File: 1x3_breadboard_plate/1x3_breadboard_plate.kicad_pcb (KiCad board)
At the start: 2 copper layers, 69.7 x 22 mm, 4 parts

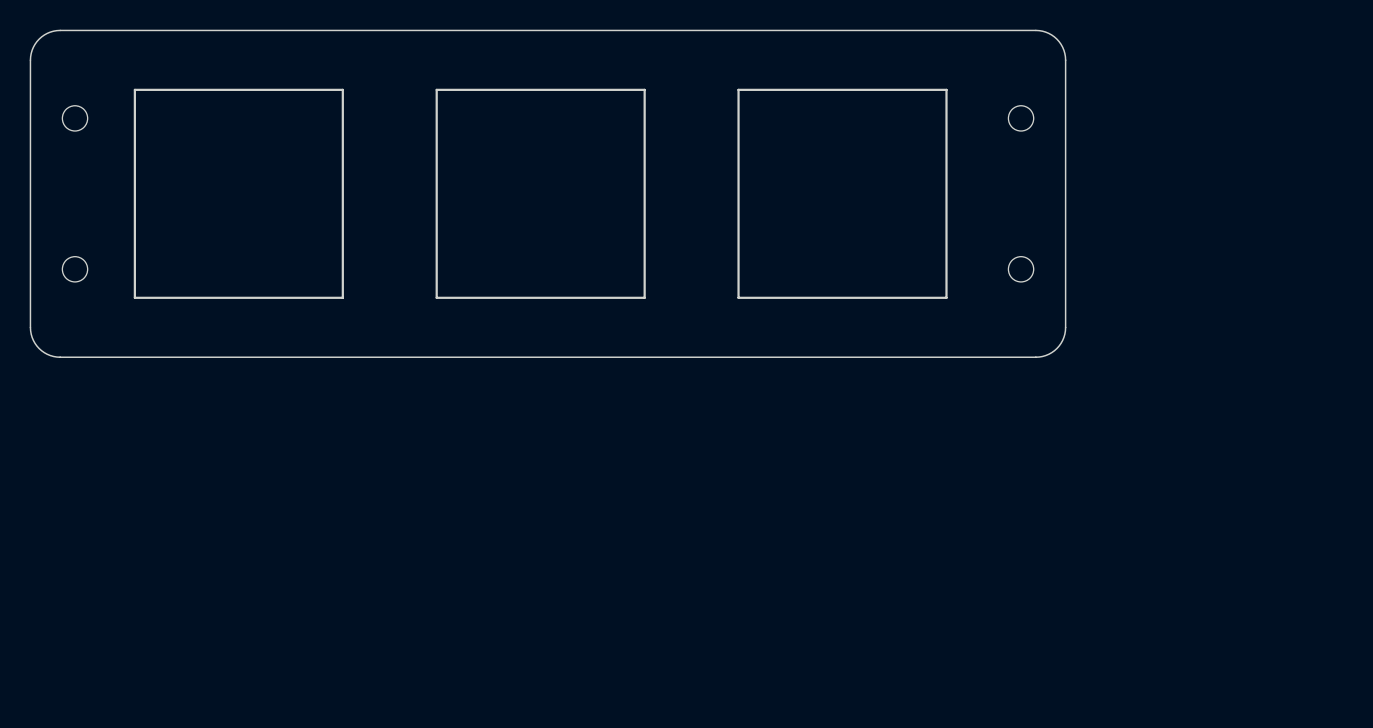
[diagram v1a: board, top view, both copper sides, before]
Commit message: fix edge cuts
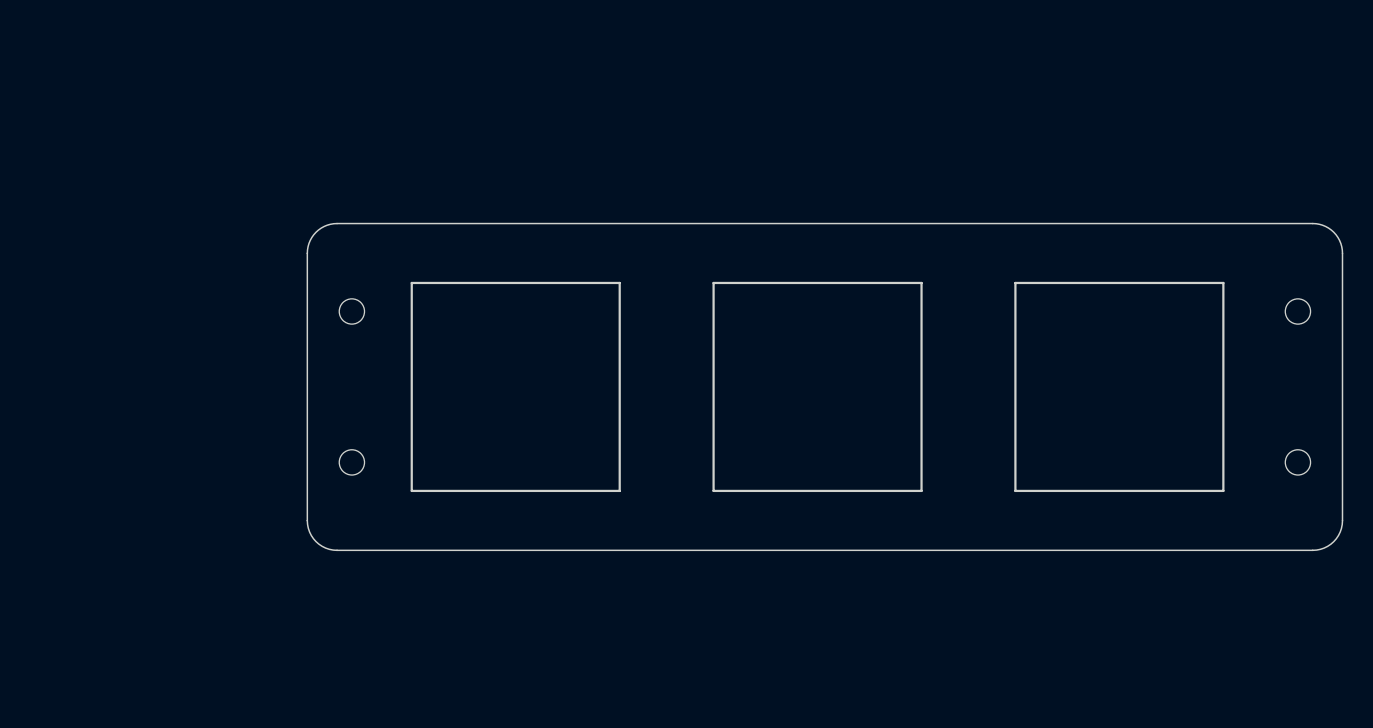
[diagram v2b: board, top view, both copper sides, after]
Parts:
- moved H1 22.7 mm to (174.7, 99.1)
- moved H2 22.7 mm to (174.7, 88.9)
- moved H1 22.7 mm to (111.0, 88.9)
- moved H2 22.7 mm to (111.0, 99.1)
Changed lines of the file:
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@@
   (net 0 "")
   (footprint "PCM_kikit:NPTH" (layer "F.Cu")
-    (at 156.019567 75.92 180)
+    (at 174.659567 88.92 180)
     (attr through_hole)
     (fp_text reference "H2" (at 0 0.5) (layer "F.SilkS") hide
@@
   )
   (footprint "PCM_kikit:NPTH" (layer "F.Cu")
-    (at 92.329567 86.08)
+    (at 110.969567 99.08)
     (attr through_hole)
     (fp_text reference "H2" (at 0 0.5) (layer "F.SilkS") hide
@@
   )
   (footprint "PCM_kikit:NPTH" (layer "F.Cu")
-    (at 92.329567 75.92)
+    (at 110.969567 88.92)
     (attr through_hole)
     (fp_text reference "H1" (at 0 0.5) (layer "F.SilkS") hide
@@
   )
   (footprint "PCM_kikit:NPTH" (layer "F.Cu")
-    (at 156.019567 86.08 180)
+    (at 174.659567 99.08 180)
     (attr through_hole)
     (fp_text reference "H1" (at 0 0.5) (layer "F.SilkS") hide
@@
     (pad "" np_thru_hole circle (at 0 0 180) (size 1.7 1.7) (drill 1.7) (layers "*.Mask"))
   )
-  (gr_arc (start 89.329567 72) (mid 89.915353 70.585786) (end 91.329567 70)
+  (gr_line (start 132.5 116.5) (end 125.5 116.5)
+    (stroke (width 0.15) (type default)) (layer "Cmts.User"))
+  (gr_arc (start 107.969567 85) (mid 108.555351 83.585775) (end 109.969567 83)
     (stroke (width 0.1) (type default)) (layer "Edge.Cuts"))
-  (gr_rect (start 137 74) (end 151 88)
+  (gr_rect (start 155.64 87) (end 169.64 101)
     (stroke (width 0.15) (type default)) (fill none) (layer "Edge.Cuts"))
-  (gr_arc (start 157.019567 70) (mid 158.433781 70.585786) (end 159.019567 72)
+  (gr_arc (start 175.659567 83) (mid 177.073802 83.585775) (end 177.659567 85)
     (stroke (width 0.1) (type default)) (layer "Edge.Cuts"))
-  (gr_arc (start 91.329567 92) (mid 89.915353 91.414214) (end 89.329567 90)
+  (gr_arc (start 109.969567 105) (mid 108.555375 104.414202) (end 107.969567 103)
     (stroke (width 0.1) (type default)) (layer "Edge.Cuts"))
-  (gr_rect (start 116.68 74) (end 130.68 88)
+  (gr_rect (start 135.32 87) (end 149.32 101)
     (stroke (width 0.15) (type default)) (fill none) (layer "Edge.Cuts"))
-  (gr_line (start 159.019567 72) (end 159.019567 90)
+  (gr_line (start 177.659567 85) (end 177.659567 103)
     (stroke (width 0.1) (type default)) (layer "Edge.Cuts"))
-  (gr_line (start 157.019567 92) (end 91.329567 92)
+  (gr_line (start 175.659567 105) (end 109.969567 105)
     (stroke (width 0.1) (type default)) (layer "Edge.Cuts"))
-  (gr_line (start 157.019567 70) (end 91.329567 70)
+  (gr_line (start 175.659567 83) (end 109.969567 83)
     (stroke (width 0.1) (type default)) (layer "Edge.Cuts"))
-  (gr_line (start 89.329567 90) (end 89.329567 72)
+  (gr_line (start 107.969567 103) (end 107.969567 85)
     (stroke (width 0.1) (type default)) (layer "Edge.Cuts"))
-  (gr_rect (start 96.36 74) (end 110.36 88)
+  (gr_rect (start 115 87) (end 129 101)
     (stroke (width 0.15) (type default)) (fill none) (layer "Edge.Cuts"))
-  (gr_arc (start 159.019567 90) (mid 158.433781 91.414214) (end 157.019567 92)
+  (gr_arc (start 177.659567 103) (mid 177.073779 104.414202) (end 175.659567 105)
     (stroke (width 0.1) (type default)) (layer "Edge.Cuts"))
-  (gr_rect (start 134.5 71.5) (end 153.5 90.5)
+  (gr_rect (start 153.14 84.5) (end 172.14 103.5)
     (stroke (width 0.15) (type default)) (fill none) (layer "Margin"))
-  (gr_rect (start 114.18 71.5) (end 133.18 90.5)
+  (gr_rect (start 132.82 84.5) (end 151.82 103.5)
     (stroke (width 0.15) (type default)) (fill none) (layer "Margin"))
-  (gr_rect (start 93.86 71.5) (end 112.86 90.5)
+  (gr_rect (start 112.5 84.5) (end 131.5 103.5)
     (stroke (width 0.15) (type default)) (fill none) (layer "Margin"))
   (zone (net 0) (net_name "") (layers "*.Mask") (hatch edge 0.5)
@@
     (polygon
       (pts
-        (xy 88 69)
-        (xy 160 69)
-        (xy 160 93)
-        (xy 88 93)
+        (xy 106.64 82)
+        (xy 178.64 82)
+        (xy 178.64 106)
+        (xy 106.64 106)
       )
     )
   )
+  (group "" (id 43b9f617-f1b2-4520-bd50-91c62da49f0e)
+    (members
+      08055c05-5de9-4a9a-a119-e19922f812c5
+      0c5f41b3-e783-4dd7-939f-8dc3d2f3ff16
+      0cdfaec3-df83-4063-ae9b-9c17142b638e
+      1a4d4f11-aa7d-4fc0-be73-470c515281a9
+      1d7a2f89-f8f4-42df-abcb-455d9649701f
+      1e90237b-85d3-4db1-a25b-07ff1cf9bf3d
+      20f8baa1-8277-4e1f-a2aa-e9319386b823
+      464e8390-9fa7-403f-ba47-4df8c322ba8b
+      5beeab23-33cb-489e-b2ee-b214e10dc540
+      71177536-c8da-41c0-92df-2cd679bc19a1
+      7d587eb0-fa47-4276-a1d8-4a22aa9f8cda
+      95e1f511-9467-4336-b604-bae186bff3ac
+      bbf3ed6e-a8e5-489c-b028-359fa569b26d
+      c9f48060-15a8-468f-8f92-c5c4dbfee1d4
+      d51c04ed-ed02-432d-bfae-dc32dd3a883f
+      da861a6b-2ef2-49cd-9050-5daf707b11a6
+      e77cc2ee-4b33-4c7b-acb0-b8ec7a6cb619
+      fd62dd3c-2c75-42d3-b98c-8bed5c4f85e8
+      fef4e613-db41-47a0-8e3a-a29de8d9e7df
+    )
+  )

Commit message: updates 1x3 breadboard plate for new dimensions
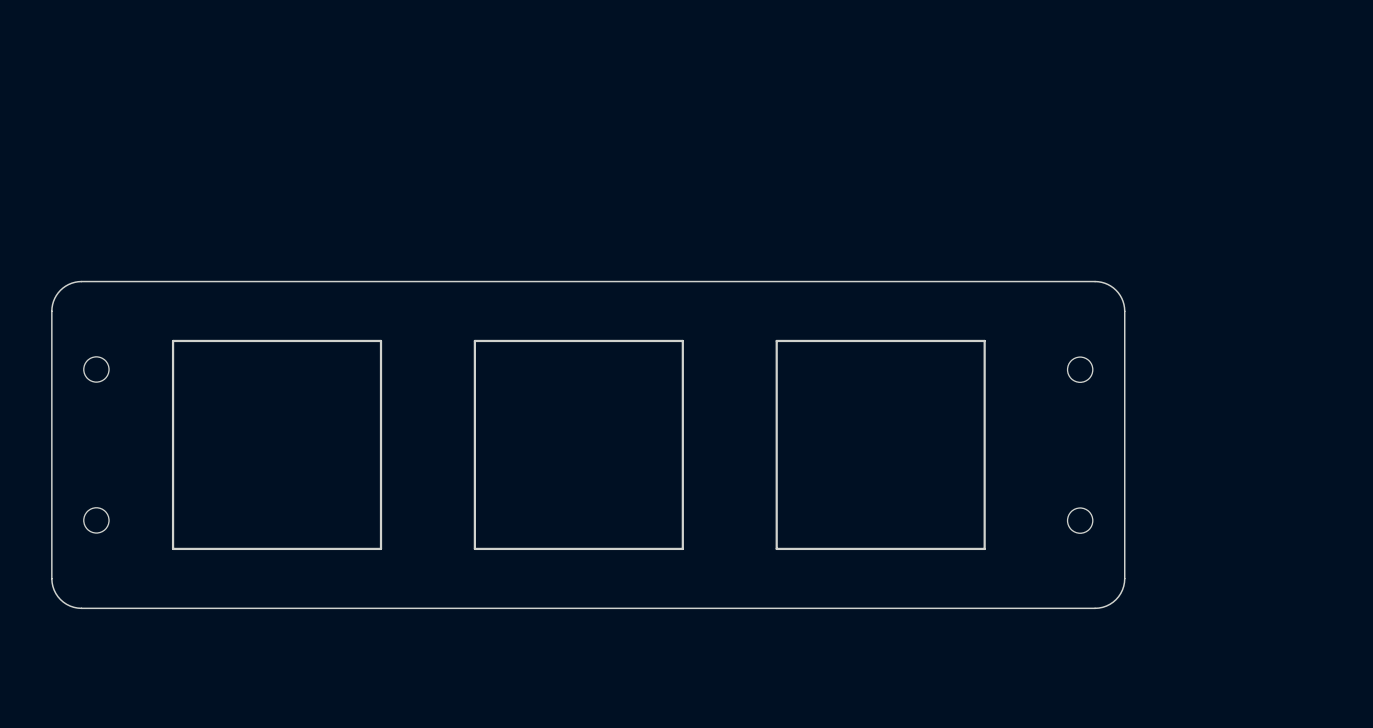
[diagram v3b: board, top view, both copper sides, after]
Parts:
- removed the H1 at (111.0, 88.9)
- removed the H1 at (174.7, 99.1)
- removed the H2 at (174.7, 88.9)
- removed the H2 at (111.0, 99.1)
- added H1: NPTH, PCM_kikit:NPTH, F.Cu at (93.8, 92.8)
- added H2: NPTH, PCM_kikit:NPTH, F.Cu at (93.8, 103.0)
- added H3: NPTH, PCM_kikit:NPTH, F.Cu at (160.0, 92.8)
- added H4: NPTH, PCM_kikit:NPTH, F.Cu at (160.0, 103.0)
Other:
- board size 69.7 x 22 mm -> 72.2 x 22 mm
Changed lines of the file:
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@@
   (net 0 "")
   (footprint "PCM_kikit:NPTH" (layer "F.Cu")
-    (at 174.659567 88.92 180)
+    (at 160 103)
     (attr through_hole)
-    (fp_text reference "H2" (at 0 0.5) (layer "F.SilkS") hide
+    (fp_text reference "H4" (at 0 0.5) (layer "F.SilkS") hide
         (effects (font (size 1 1) (thickness 0.15)))
     )
@@
         (effects (font (size 1 1) (thickness 0.15)))
     )
-    (pad "" np_thru_hole circle (at 0 0 180) (size 1.7 1.7) (drill 1.7) (layers "*.Mask"))
+    (pad "" np_thru_hole circle (at 0 0) (size 1.7 1.7) (drill 1.7) (layers "*.Mask"))
   )
   (footprint "PCM_kikit:NPTH" (layer "F.Cu")
-    (at 110.969567 99.08)
+    (at 93.77 92.825)
+    (attr through_hole)
+    (fp_text reference "H1" (at 0 0.5) (layer "F.SilkS") hide
+        (effects (font (size 1 1) (thickness 0.15)))
+    )
+    (fp_text value "NPTH" (at 0 -0.5) (layer "F.Fab") hide
+        (effects (font (size 1 1) (thickness 0.15)))
+    )
+    (pad "" np_thru_hole circle (at 0 0) (size 1.7 1.7) (drill 1.7) (layers "*.Mask"))
+  )
+  (footprint "PCM_kikit:NPTH" (layer "F.Cu")
+    (at 93.77 102.985)
     (attr through_hole)
     (fp_text reference "H2" (at 0 0.5) (layer "F.SilkS") hide
@@
   )
   (footprint "PCM_kikit:NPTH" (layer "F.Cu")
-    (at 110.969567 88.92)
+    (at 160 92.84)
     (attr through_hole)
-    (fp_text reference "H1" (at 0 0.5) (layer "F.SilkS") hide
+    (fp_text reference "H3" (at 0 0.5) (layer "F.SilkS") hide
         (effects (font (size 1 1) (thickness 0.15)))
     )
@@
     (pad "" np_thru_hole circle (at 0 0) (size 1.7 1.7) (drill 1.7) (layers "*.Mask"))
   )
-  (footprint "PCM_kikit:NPTH" (layer "F.Cu")
-    (at 174.659567 99.08 180)
-    (attr through_hole)
-    (fp_text reference "H1" (at 0 0.5) (layer "F.SilkS") hide
-        (effects (font (size 1 1) (thickness 0.15)))
-    )
-    (fp_text value "NPTH" (at 0 -0.5) (layer "F.Fab") hide
-        (effects (font (size 1 1) (thickness 0.15)))
-    )
-    (pad "" np_thru_hole circle (at 0 0 180) (size 1.7 1.7) (drill 1.7) (layers "*.Mask"))
-  )
-  (gr_line (start 132.5 116.5) (end 125.5 116.5)
-    (stroke (width 0.15) (type default)) (layer "Cmts.User"))
-  (gr_arc (start 107.969567 85) (mid 108.555351 83.585775) (end 109.969567 83)
+  (gr_arc (start 129.540026 124.705) (mid 127.54 122.705) (end 129.540026 120.705)
+    (stroke (width 0.15) (type default)) (layer "Dwgs.User"))
+  (gr_arc (start 110.48997 120.705) (mid 112.49 122.705) (end 110.48997 124.705)
+    (stroke (width 0.15) (type default)) (layer "Dwgs.User"))
+  (gr_arc (start 90.77 88.905) (mid 91.355784 87.490775) (end 92.77 86.905)
     (stroke (width 0.1) (type default)) (layer "Edge.Cuts"))
-  (gr_rect (start 155.64 87) (end 169.64 101)
+  (gr_rect (start 139.57 90.905) (end 153.57 104.905)
     (stroke (width 0.15) (type default)) (fill none) (layer "Edge.Cuts"))
-  (gr_arc (start 175.659567 83) (mid 177.073802 83.585775) (end 177.659567 85)
+  (gr_arc (start 161 86.905) (mid 162.414235 87.490775) (end 163 88.905)
     (stroke (width 0.1) (type default)) (layer "Edge.Cuts"))
-  (gr_arc (start 109.969567 105) (mid 108.555375 104.414202) (end 107.969567 103)
+  (gr_arc (start 92.77 108.905) (mid 91.355808 108.319202) (end 90.77 106.905)
     (stroke (width 0.1) (type default)) (layer "Edge.Cuts"))
-  (gr_rect (start 135.32 87) (end 149.32 101)
+  (gr_rect (start 119.25 90.905) (end 133.25 104.905)
     (stroke (width 0.15) (type default)) (fill none) (layer "Edge.Cuts"))
-  (gr_line (start 177.659567 85) (end 177.659567 103)
+  (gr_line (start 163 88.905) (end 163 106.905)
     (stroke (width 0.1) (type default)) (layer "Edge.Cuts"))
-  (gr_line (start 175.659567 105) (end 109.969567 105)
+  (gr_line (start 161 108.905) (end 92.77 108.905)
     (stroke (width 0.1) (type default)) (layer "Edge.Cuts"))
-  (gr_line (start 175.659567 83) (end 109.969567 83)
+  (gr_line (start 161 86.905) (end 92.77 86.905)
     (stroke (width 0.1) (type default)) (layer "Edge.Cuts"))
-  (gr_line (start 107.969567 103) (end 107.969567 85)
+  (gr_line (start 90.77 106.905) (end 90.77 88.905)
     (stroke (width 0.1) (type default)) (layer "Edge.Cuts"))
-  (gr_rect (start 115 87) (end 129 101)
+  (gr_rect (start 98.93 90.905) (end 112.93 104.905)
     (stroke (width 0.15) (type default)) (fill none) (layer "Edge.Cuts"))
-  (gr_arc (start 177.659567 103) (mid 177.073779 104.414202) (end 175.659567 105)
+  (gr_arc (start 163 106.905) (mid 162.414212 108.319202) (end 161 108.905)
     (stroke (width 0.1) (type default)) (layer "Edge.Cuts"))
-  (gr_rect (start 153.14 84.5) (end 172.14 103.5)
+  (gr_rect (start 140.995 81.94) (end 159.995 100.94)
     (stroke (width 0.15) (type default)) (fill none) (layer "Margin"))
-  (gr_rect (start 132.82 84.5) (end 151.82 103.5)
+  (gr_rect (start 120.675 81.94) (end 139.675 100.94)
     (stroke (width 0.15) (type default)) (fill none) (layer "Margin"))
-  (gr_rect (start 112.5 84.5) (end 131.5 103.5)
+  (gr_rect (start 100.355 81.94) (end 119.355 100.94)
     (stroke (width 0.15) (type default)) (fill none) (layer "Margin"))
   (zone (net 0) (net_name "") (layers "*.Mask") (hatch edge 0.5)
@@
     (polygon
       (pts
-        (xy 106.64 82)
-        (xy 178.64 82)
-        (xy 178.64 106)
-        (xy 106.64 106)
+        (xy 90 86)
+        (xy 164 86)
+        (xy 164 110)
+        (xy 90 110)
       )
     )
   )
-  (group "" (id 43b9f617-f1b2-4520-bd50-91c62da49f0e)
-    (members
-      08055c05-5de9-4a9a-a119-e19922f812c5
-      0c5f41b3-e783-4dd7-939f-8dc3d2f3ff16
-      0cdfaec3-df83-4063-ae9b-9c17142b638e
-      1a4d4f11-aa7d-4fc0-be73-470c515281a9
-      1d7a2f89-f8f4-42df-abcb-455d9649701f
-      1e90237b-85d3-4db1-a25b-07ff1cf9bf3d
-      20f8baa1-8277-4e1f-a2aa-e9319386b823
-      464e8390-9fa7-403f-ba47-4df8c322ba8b
-      5beeab23-33cb-489e-b2ee-b214e10dc540
-      71177536-c8da-41c0-92df-2cd679bc19a1
-      7d587eb0-fa47-4276-a1d8-4a22aa9f8cda
-      95e1f511-9467-4336-b604-bae186bff3ac
-      bbf3ed6e-a8e5-489c-b028-359fa569b26d
-      c9f48060-15a8-468f-8f92-c5c4dbfee1d4
-      d51c04ed-ed02-432d-bfae-dc32dd3a883f
-      da861a6b-2ef2-49cd-9050-5daf707b11a6
-      e77cc2ee-4b33-4c7b-acb0-b8ec7a6cb619
-      fd62dd3c-2c75-42d3-b98c-8bed5c4f85e8
-      fef4e613-db41-47a0-8e3a-a29de8d9e7df
-    )
-  )
